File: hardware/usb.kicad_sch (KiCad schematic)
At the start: 44 parts

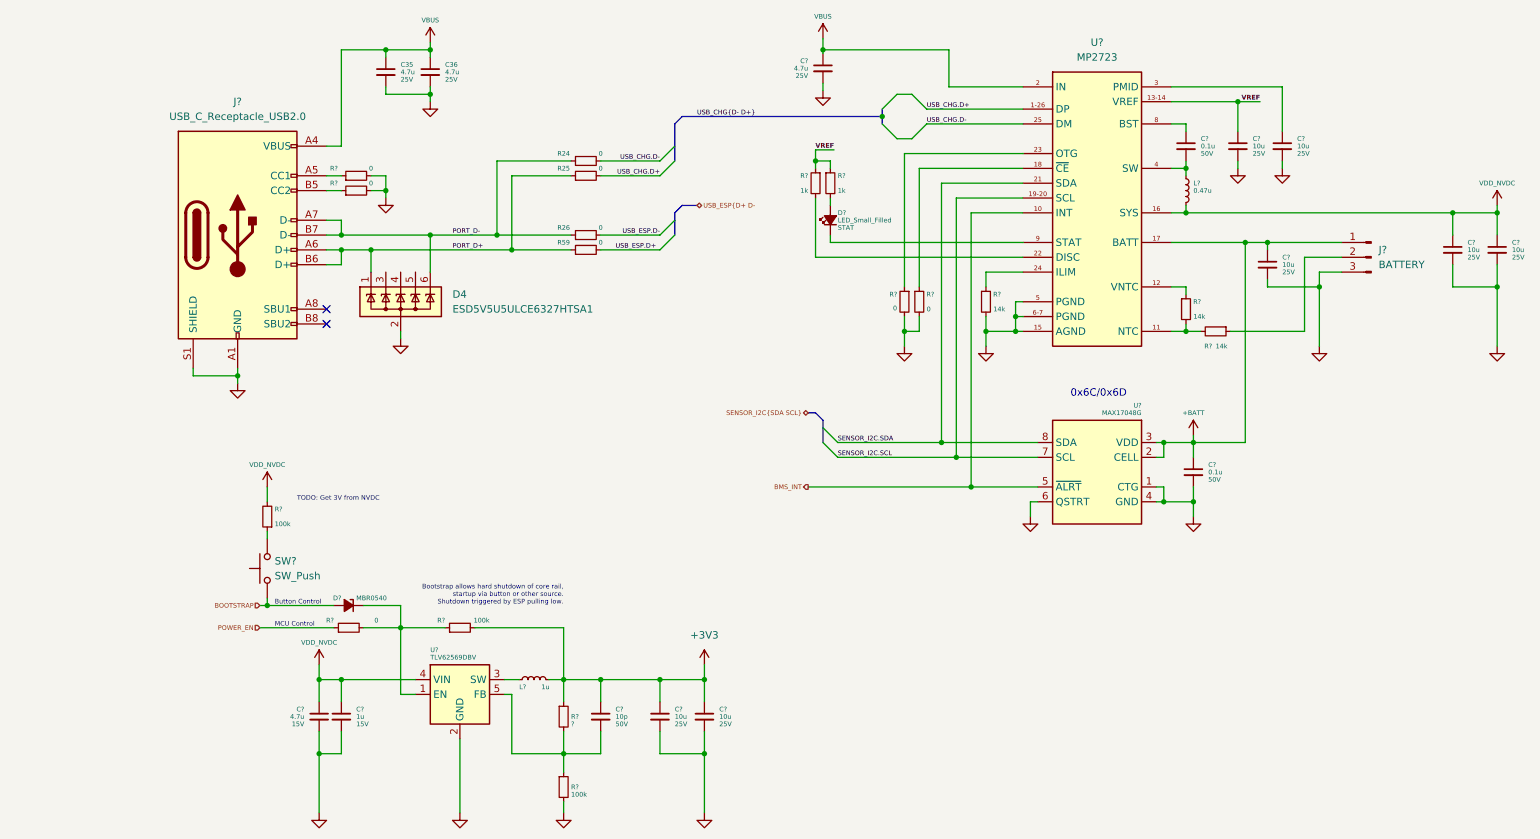
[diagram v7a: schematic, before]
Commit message: layout 0 unconnected
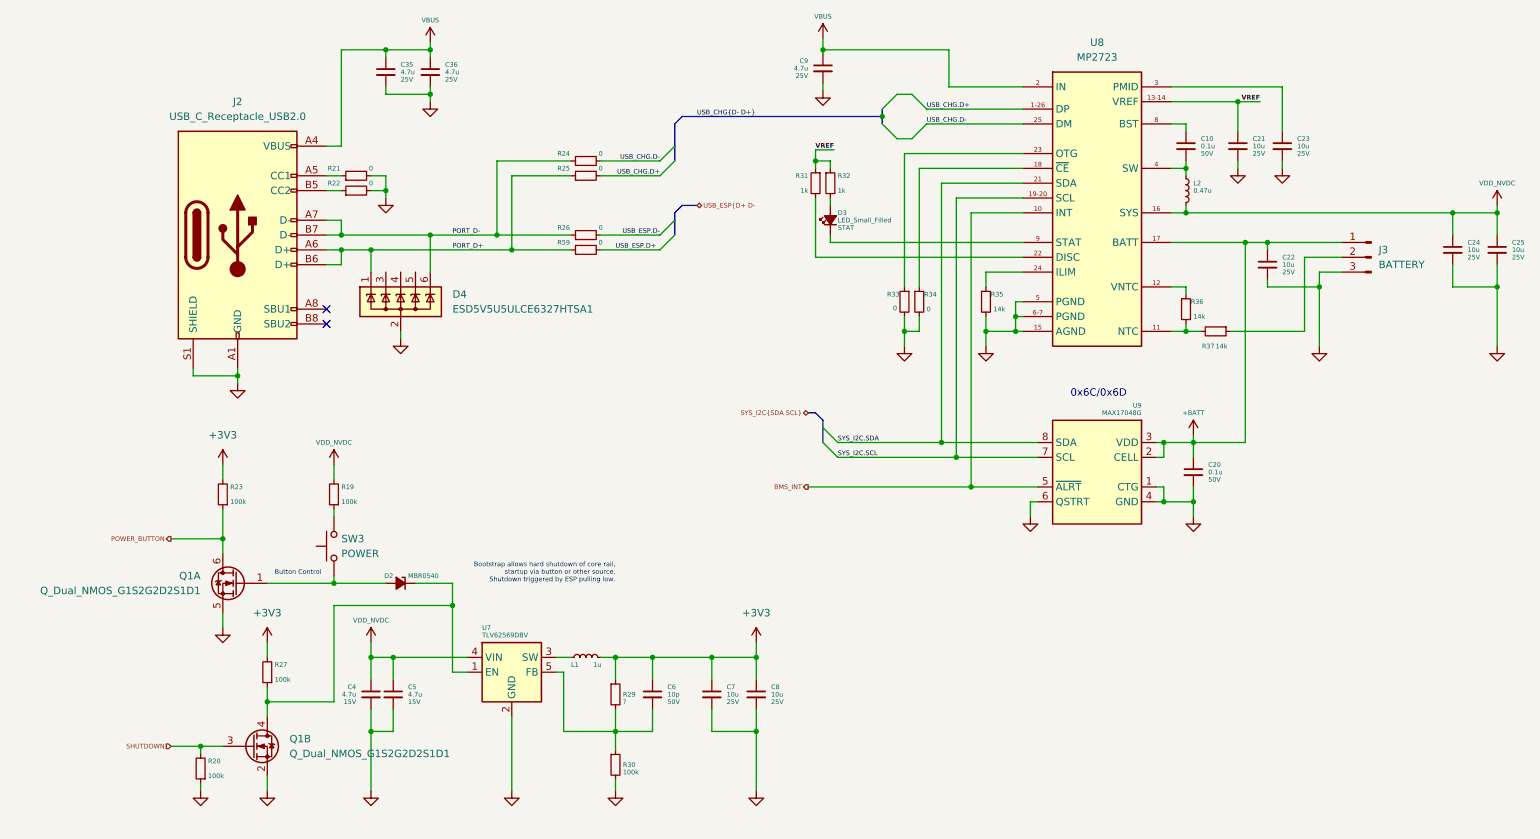
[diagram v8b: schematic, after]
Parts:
- removed C?: 1u, Capacitor_SMD:C_0402_1005Metric, symbol Device:C_Small
- removed R?: 100k, Resistor_SMD:R_0402_1005Metric, symbol Device:R_Small
- removed R?: 0, Resistor_SMD:R_0402_1005Metric, symbol Device:R_Small
- added C5: 4.7u, Capacitor_SMD:C_0603_1608Metric, symbol Device:C_Small
- added Q1: Q_Dual_NMOS_G1S2G2D2S1D1, symbol Device:Q_Dual_NMOS_G1S2G2D2S1D1
- added R20, R23, R27: 100k, Resistor_SMD:R_0402_1005Metric, symbol Device:R_Small
- J2: renamed from J?; footprint (none) -> Connector_USB:USB_C_Receptacle_HRO_TYPE-C-31-M-12
- J3: renamed from J?; footprint (none) -> Connector_PinHeader_1.27mm:PinHeader_1x03_P1.27mm_Vertical
- SW3: renamed from SW?; value SW_Push -> POWER; footprint (none) -> Button_Switch_SMD:SW_SPST_B3U-1000P
- gave numbers to parts that had none: 31
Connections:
- net +3V3: now also R23.2, R27.2
- net GND: now also U9.9 (PAD), C5.2, Q1.2 (S), Q1.5 (S), R20.1
- net VDD_NVDC: now also C5.1
- net at D2.1 (K), U7.1 (EN): now also Q1.4 (D), R27.1
- net BOOTSTRAP: no longer names the net of D2.2 (A), SW3.2
- net BOOTSTRAP: now also Q1.1 (G)
- net SENSOR_I2C.SCL renamed SYS_I2C.SCL
- net SENSOR_I2C.SDA renamed SYS_I2C.SDA
- new net POWER_BUTTON: Q1.6 (D), R23.1
- new net SHUTDOWN: Q1.3 (G), R20.2
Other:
- note removed: "MCU Control"
- note removed: "TODO: Get 3V from NVDC"
- moved on the sheet: C4, C6, C7, C8, D2, L1, R19, R29, R30, SW3, U7
